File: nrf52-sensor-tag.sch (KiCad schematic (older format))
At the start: 20 parts, among them IC1 ISP1807-LR-RS, IC2 MAX44009EDT+T, U1 BME280

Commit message: Moved components and routed the board
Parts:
- removed R?: 10k, Resistor_SMD:R_0603_1608Metric, symbol Device:R_Small
- removed U?: MAX811REUS-T, Package_TO_SOT_SMD:SOT-143, symbol Power_Supervisor:MAX811REUS-T
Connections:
- net labels removed: BATLOW
- wire segments 76 -> 70
- no-connect marks 40 -> 39
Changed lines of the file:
@@
 Wire Wire Line
 	5050 3500 5300 3500
-$Comp
-L Power_Supervisor:MAX811REUS-T U?
-U 1 1 601F6A74
-P 5350 6600
-F 0 "U?" H 5600 7000 50  0000 L CNN
-F 1 "MAX811REUS-T" H 5500 6900 50  0000 L CNN
-F 2 "Package_TO_SOT_SMD:SOT-143" H 5450 6300 50  0001 L CNN
-F 3 "https://datasheets.maximintegrated.com/en/ds/MAX811-MAX812.pdf" H 5000 5900 50  0001 C CNN
-	1    5350 6600
-	1    0    0    -1
-$EndComp
-Text Label 6150 6600 2    50   ~ 0
-BATLOW
-Wire Wire Line
-	6150 6600 5750 6600
-Text Label 5150 6200 0    50   ~ 0
-VCC
-Wire Wire Line
-	5150 6200 5350 6200
-Wire Wire Line
-	5350 6200 5350 6300
-NoConn ~ 4950 6600
-$Comp
-L power:GND #PWR?
-U 1 1 601FE059
-P 5350 6900
-F 0 "#PWR?" H 5350 6650 50  0001 C CNN
-F 1 "GND" H 5355 6727 50  0000 C CNN
-F 2 "" H 5350 6900 50  0001 C CNN
-F 3 "" H 5350 6900 50  0001 C CNN
-	1    5350 6900
-	1    0    0    -1
-$EndComp
-$Comp
-L Device:R_Small R?
-U 1 1 601FEA86
-P 6250 5750
-F 0 "R?" V 6054 5750 50  0000 C CNN
-F 1 "10k" V 6145 5750 50  0000 C CNN
-F 2 "Resistor_SMD:R_0603_1608Metric" H 6250 5750 50  0001 C CNN
-F 3 "~" H 6250 5750 50  0001 C CNN
-	1    6250 5750
-	0    1    1    0
-$EndComp
-Text Label 5750 5750 0    50   ~ 0
-BATLOW
-$Comp
-L power:GND #PWR?
-U 1 1 601FEFB1
-P 6600 5800
-F 0 "#PWR?" H 6600 5550 50  0001 C CNN
-F 1 "GND" H 6605 5627 50  0000 C CNN
-F 2 "" H 6600 5800 50  0001 C CNN
-F 3 "" H 6600 5800 50  0001 C CNN
-	1    6600 5800
-	1    0    0    -1
-$EndComp
-Wire Wire Line
-	5750 5750 6150 5750
-Wire Wire Line
-	6350 5750 6600 5750
-Wire Wire Line
-	6600 5750 6600 5800
 $EndSCHEMATC

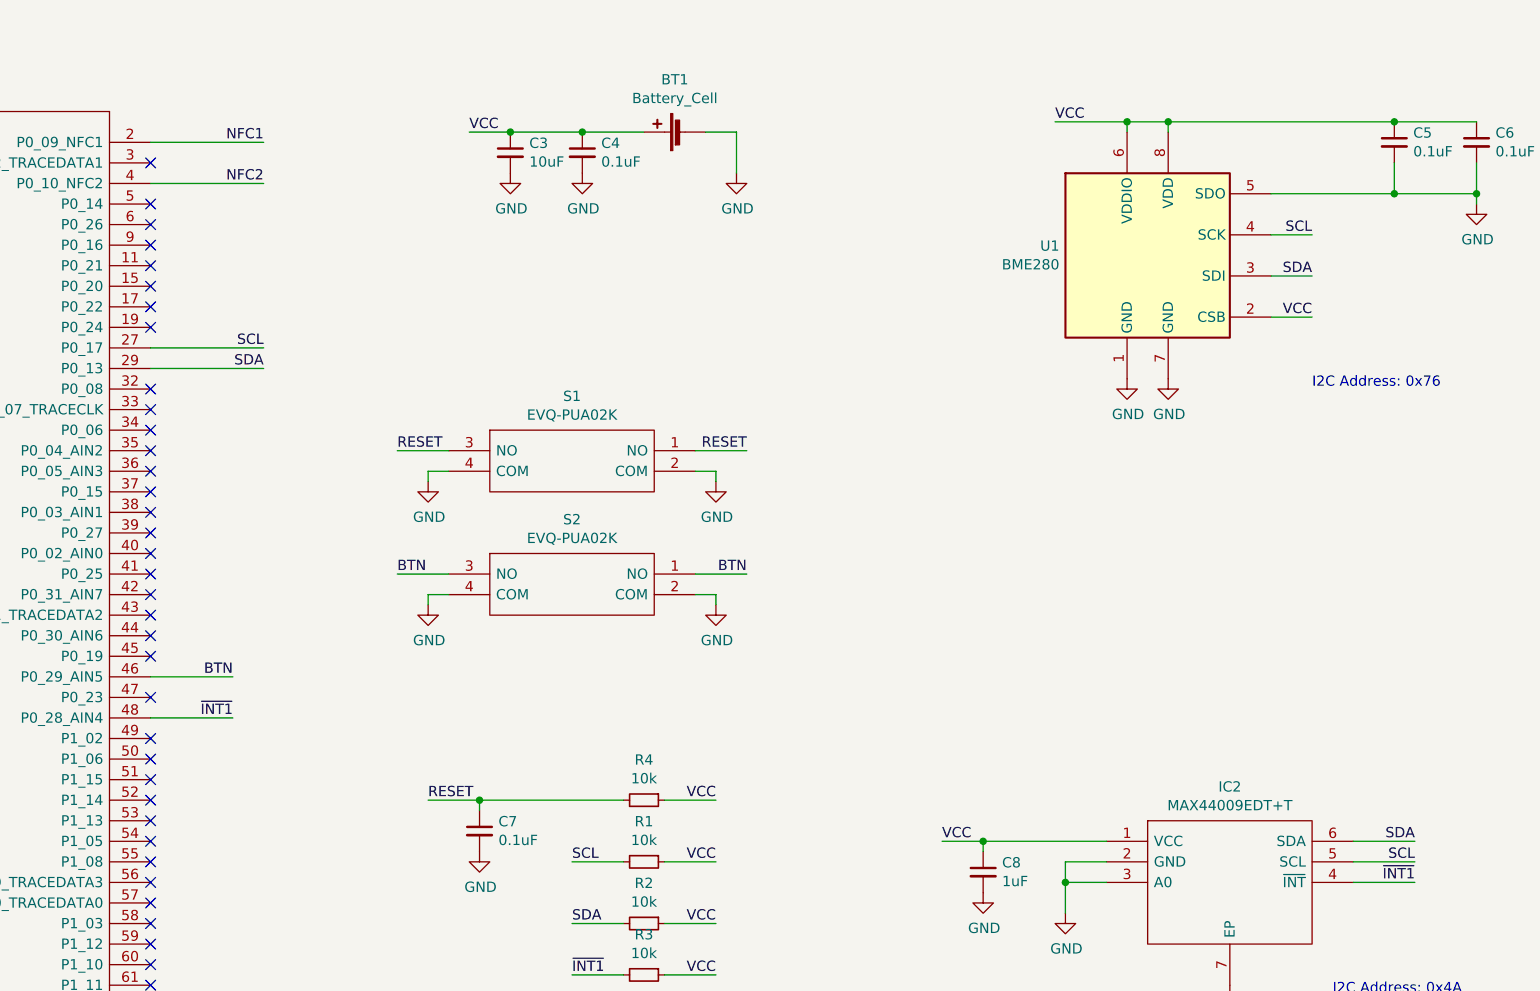
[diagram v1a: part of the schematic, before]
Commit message: Attached the sensors VCC to GPIOs of the nrf instead vcc (incl. a jumper just in case)
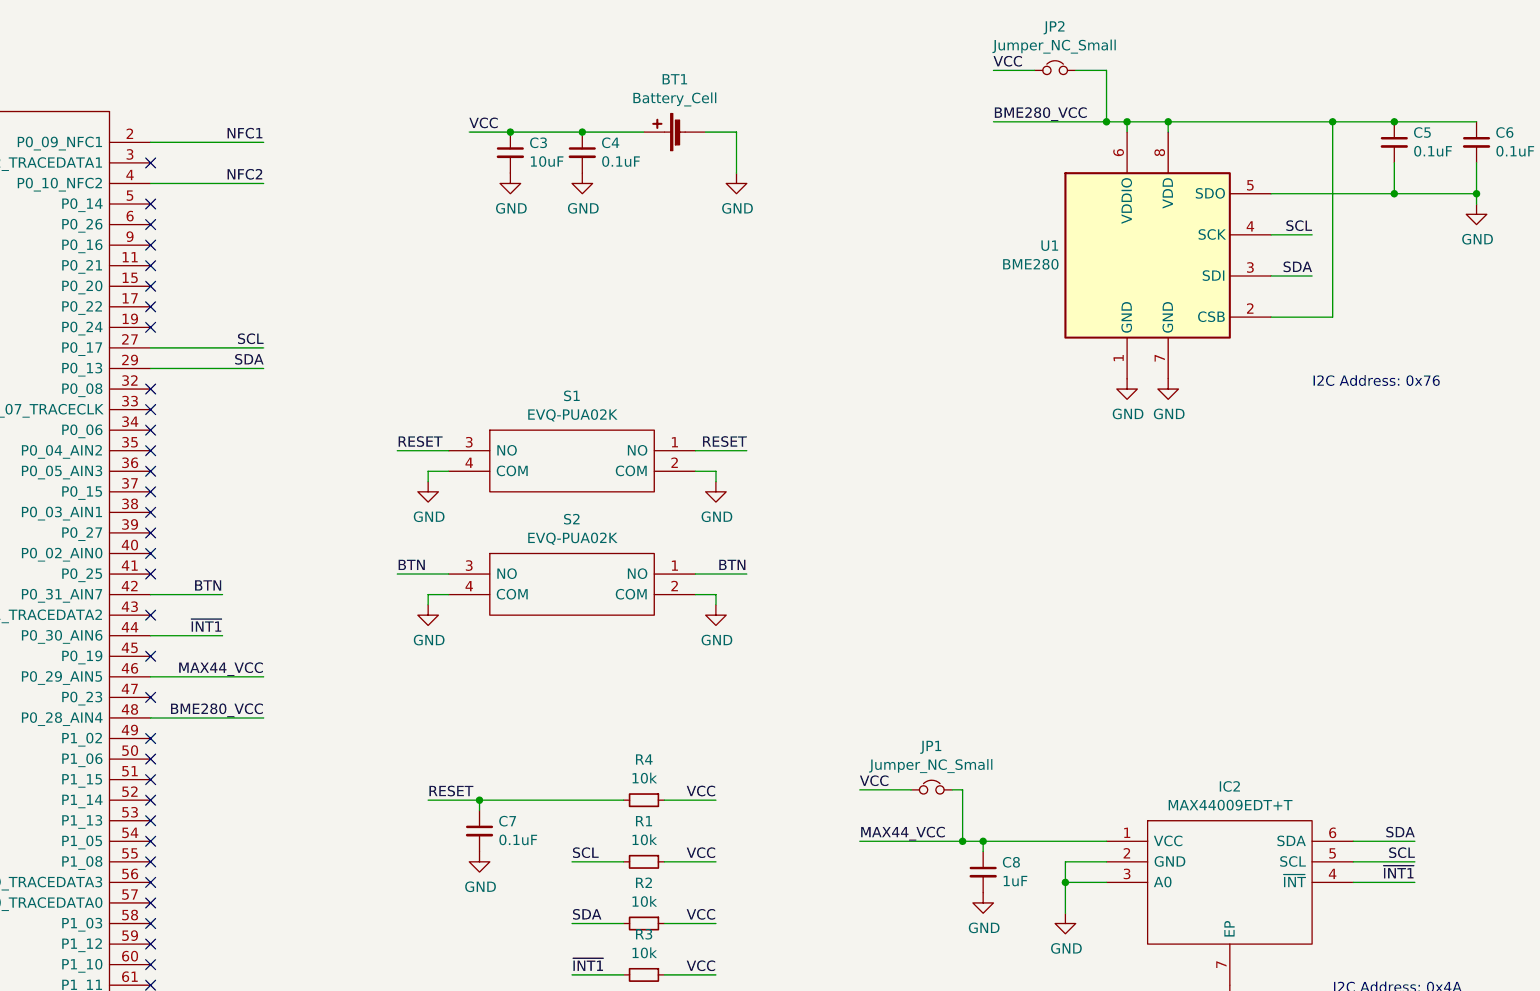
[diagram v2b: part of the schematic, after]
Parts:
- added JP1, JP2: Jumper_NC_Small, Jumper:SolderJumper-2_P1.3mm_Open_TrianglePad1.0x1.5mm, symbol Device:Jumper_NC_Small
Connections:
- net BTN: now also IC1.42 (P0_31_AIN7); no longer IC1.46 (P0_29_AIN5)
- net VCC: now also JP1.1, JP2.1; no longer C5.1, C6.1, C8.1, IC2.1 (VCC), U1.2 (CSB), U1.6 (VDDIO), U1.8 (VDD)
- net ~INT1: now also IC1.44 (P0_30_AIN6); no longer IC1.48 (P0_28_AIN4)
- new net BME280_VCC: C5.1, C6.1, IC1.48 (P0_28_AIN4), JP2.2, U1.2 (CSB), U1.6 (VDDIO), U1.8 (VDD)
- new net MAX44_VCC: C8.1, IC1.46 (P0_29_AIN5), IC2.1 (VCC), JP1.2
- no-connect marks 39 -> 37
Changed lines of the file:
@@
 	1    0    0    -1
 $EndComp
-Text Label 8250 1300 0    50   ~ 0
-VCC
+Text Label 7950 1300 0    50   ~ 0
+BME280_VCC
 Wire Wire Line
 	8600 1350 8600 1300
-Wire Wire Line
-	8600 1300 8250 1300
 Wire Wire Line
 	8800 1350 8800 1300
@@
 	8600 1300 8800 1300
 Wire Wire Line
-	8800 1300 9900 1300
+	8800 1300 9600 1300
 Connection ~ 8800 1300
 Connection ~ 9900 1300
@@
 Text Label 6600 5200 2    50   ~ 0
 VCC
-Text Label 9500 2250 2    50   ~ 0
-VCC
-Wire Wire Line
-	9500 2250 9300 2250
 Wire Wire Line
 	5900 4900 6150 4900
@@
 Wire Wire Line
 	6600 4900 6350 4900
-Text Label 7700 4800 0    50   ~ 0
-VCC
+Text Label 7300 4800 0    50   ~ 0
+MAX44_VCC
 $Comp
 L power:GND #PWR0105
@@
 	1    0    0    -1
 $EndComp
-Wire Wire Line
-	7700 4800 7900 4800
 Wire Wire Line
 	7900 4850 7900 4800
@@
 NoConn ~ 3850 3400
 NoConn ~ 3850 3500
-NoConn ~ 3850 3600
 NoConn ~ 3850 3700
-NoConn ~ 3850 3800
 NoConn ~ 3850 3900
 NoConn ~ 3850 4100
@@
 NoConn ~ 3850 5700
 NoConn ~ 3850 5800
-Text Label 4250 4200 2    50   ~ 0
+Text Label 4200 3800 2    50   ~ 0
 ~INT1
-Wire Wire Line
-	4250 4200 3850 4200
 $Comp
 L EVQ-PUA02K:EVQ-PUA02K S1
@@
 	1    0    0    -1
 $EndComp
-Text Label 4250 4000 2    50   ~ 0
+Text Label 4200 3600 2    50   ~ 0
 BTN
-Wire Wire Line
-	4250 4000 3850 4000
 Text Label 6750 3500 2    50   ~ 0
 BTN
@@
 Wire Wire Line
 	5050 3500 5300 3500
+Wire Wire Line
+	7950 1300 8500 1300
+Wire Wire Line
+	4200 3600 3850 3600
+Wire Wire Line
+	4200 3800 3850 3800
+Text Label 4400 4000 2    50   ~ 0
+MAX44_VCC
+Text Label 4400 4200 2    50   ~ 0
+BME280_VCC
+Wire Wire Line
+	3850 4200 4400 4200
+Wire Wire Line
+	3850 4000 4400 4000
+$Comp
+L Device:Jumper_NC_Small JP2
+U 1 1 6023FE8E
+P 8250 1050
+F 0 "JP2" H 8250 1262 50  0000 C CNN
+F 1 "Jumper_NC_Small" H 8250 1171 50  0000 C CNN
+F 2 "Jumper:SolderJumper-2_P1.3mm_Open_TrianglePad1.0x1.5mm" H 8250 1050 50  0001 C CNN
+F 3 "~" H 8250 1050 50  0001 C CNN
+	1    8250 1050
+	1    0    0    -1
+$EndComp
+$Comp
+L Device:Jumper_NC_Small JP1
+U 1 1 60240E97
+P 7650 4550
+F 0 "JP1" H 7650 4762 50  0000 C CNN
+F 1 "Jumper_NC_Small" H 7650 4671 50  0000 C CNN
+F 2 "Jumper:SolderJumper-2_P1.3mm_Open_TrianglePad1.0x1.5mm" H 7650 4550 50  0001 C CNN
+F 3 "~" H 7650 4550 50  0001 C CNN
+	1    7650 4550
+	1    0    0    -1
+$EndComp
+Text Label 7300 4550 0    50   ~ 0
+VCC
+Wire Wire Line
+	7300 4550 7550 4550
+Wire Wire Line
+	7300 4800 7800 4800
+Wire Wire Line
+	7750 4550 7800 4550
+Wire Wire Line
+	7800 4550 7800 4800
+Connection ~ 7800 4800
+Wire Wire Line
+	7800 4800 7900 4800
+Text Label 7950 1050 0    50   ~ 0
+VCC
+Wire Wire Line
+	7950 1050 8150 1050
+Wire Wire Line
+	8350 1050 8500 1050
+Wire Wire Line
+	8500 1050 8500 1300
+Connection ~ 8500 1300
+Wire Wire Line
+	8500 1300 8600 1300
+Wire Wire Line
+	9600 2250 9600 1300
+Wire Wire Line
+	9300 2250 9600 2250
+Connection ~ 9600 1300
+Wire Wire Line
+	9600 1300 9900 1300
 $EndSCHEMATC

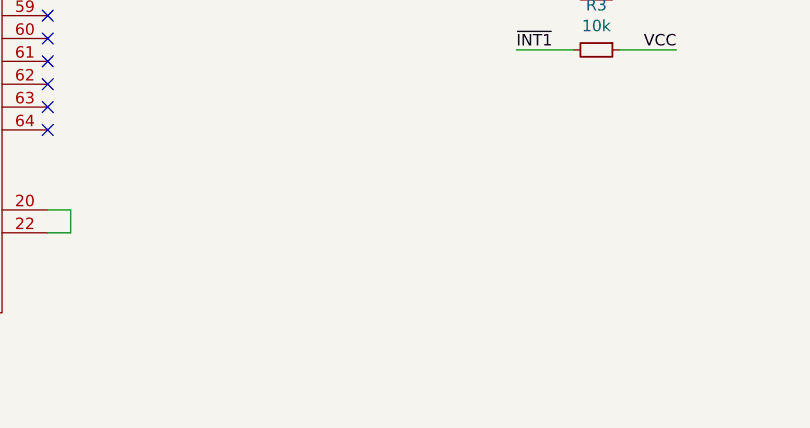
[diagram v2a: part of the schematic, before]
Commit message: Add debug connector
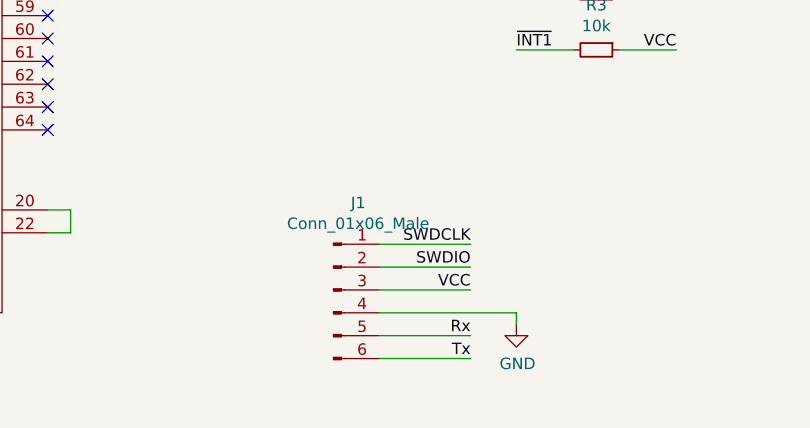
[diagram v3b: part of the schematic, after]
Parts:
- added J1: Conn_01x06_Male, Connector_PinHeader_2.00mm:PinHeader_1x06_P2.00mm_Vertical, symbol Connector:Conn_01x06_Male
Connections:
- net GND: now also J1.4 (Pin_4)
- net SWDCLK: now also J1.1 (Pin_1)
- net SWDIO: now also J1.2 (Pin_2)
- net VCC: now also J1.3 (Pin_3)
- new net Rx: J1.5 (Pin_5)
- new net Tx: J1.6 (Pin_6)
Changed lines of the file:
@@
 Wire Wire Line
 	9600 1300 9900 1300
+$Comp
+L Connector:Conn_01x06_Male J1
+U 1 1 6020A1D2
+P 5100 6500
+F 0 "J1" H 5208 6881 50  0000 C CNN
+F 1 "Conn_01x06_Male" H 5208 6790 50  0000 C CNN
+F 2 "Connector_PinHeader_2.00mm:PinHeader_1x06_P2.00mm_Vertical" H 5100 6500 50  0001 C CNN
+F 3 "~" H 5100 6500 50  0001 C CNN
+	1    5100 6500
+	1    0    0    -1
+$EndComp
+Text Label 5700 6400 2    50   ~ 0
+SWDIO
+Text Label 5700 6300 2    50   ~ 0
+SWDCLK
+Text Label 5700 6500 2    50   ~ 0
+VCC
+$Comp
+L power:GND #PWR0118
+U 1 1 6020BEB6
+P 5900 6650
+F 0 "#PWR0118" H 5900 6400 50  0001 C CNN
+F 1 "GND" H 5905 6477 50  0000 C CNN
+F 2 "" H 5900 6650 50  0001 C CNN
+F 3 "" H 5900 6650 50  0001 C CNN
+	1    5900 6650
+	1    0    0    -1
+$EndComp
+Wire Wire Line
+	5300 6600 5900 6600
+Wire Wire Line
+	5700 6500 5300 6500
+Wire Wire Line
+	5300 6400 5700 6400
+Wire Wire Line
+	5700 6300 5300 6300
+Wire Wire Line
+	5900 6650 5900 6600
+Text Label 5700 6800 2    50   ~ 0
+Tx
+Text Label 5700 6700 2    50   ~ 0
+Rx
+Wire Wire Line
+	5700 6700 5300 6700
+Wire Wire Line
+	5700 6800 5300 6800
 $EndSCHEMATC

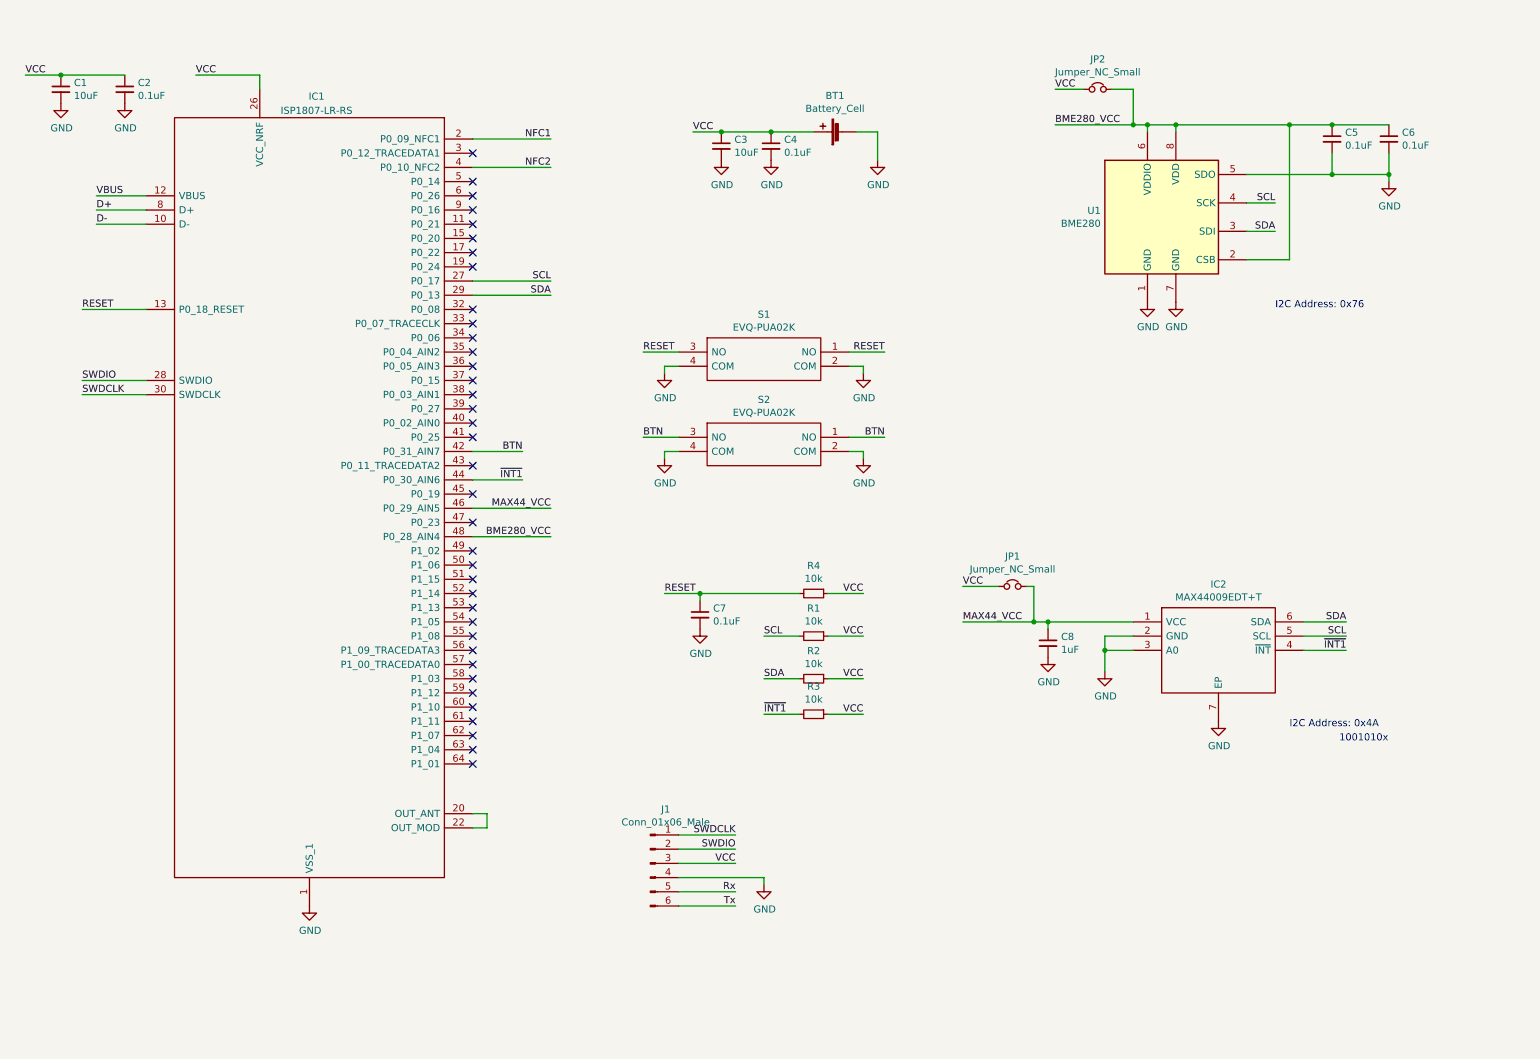
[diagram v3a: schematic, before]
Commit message: Beautify schematics + added debug connector
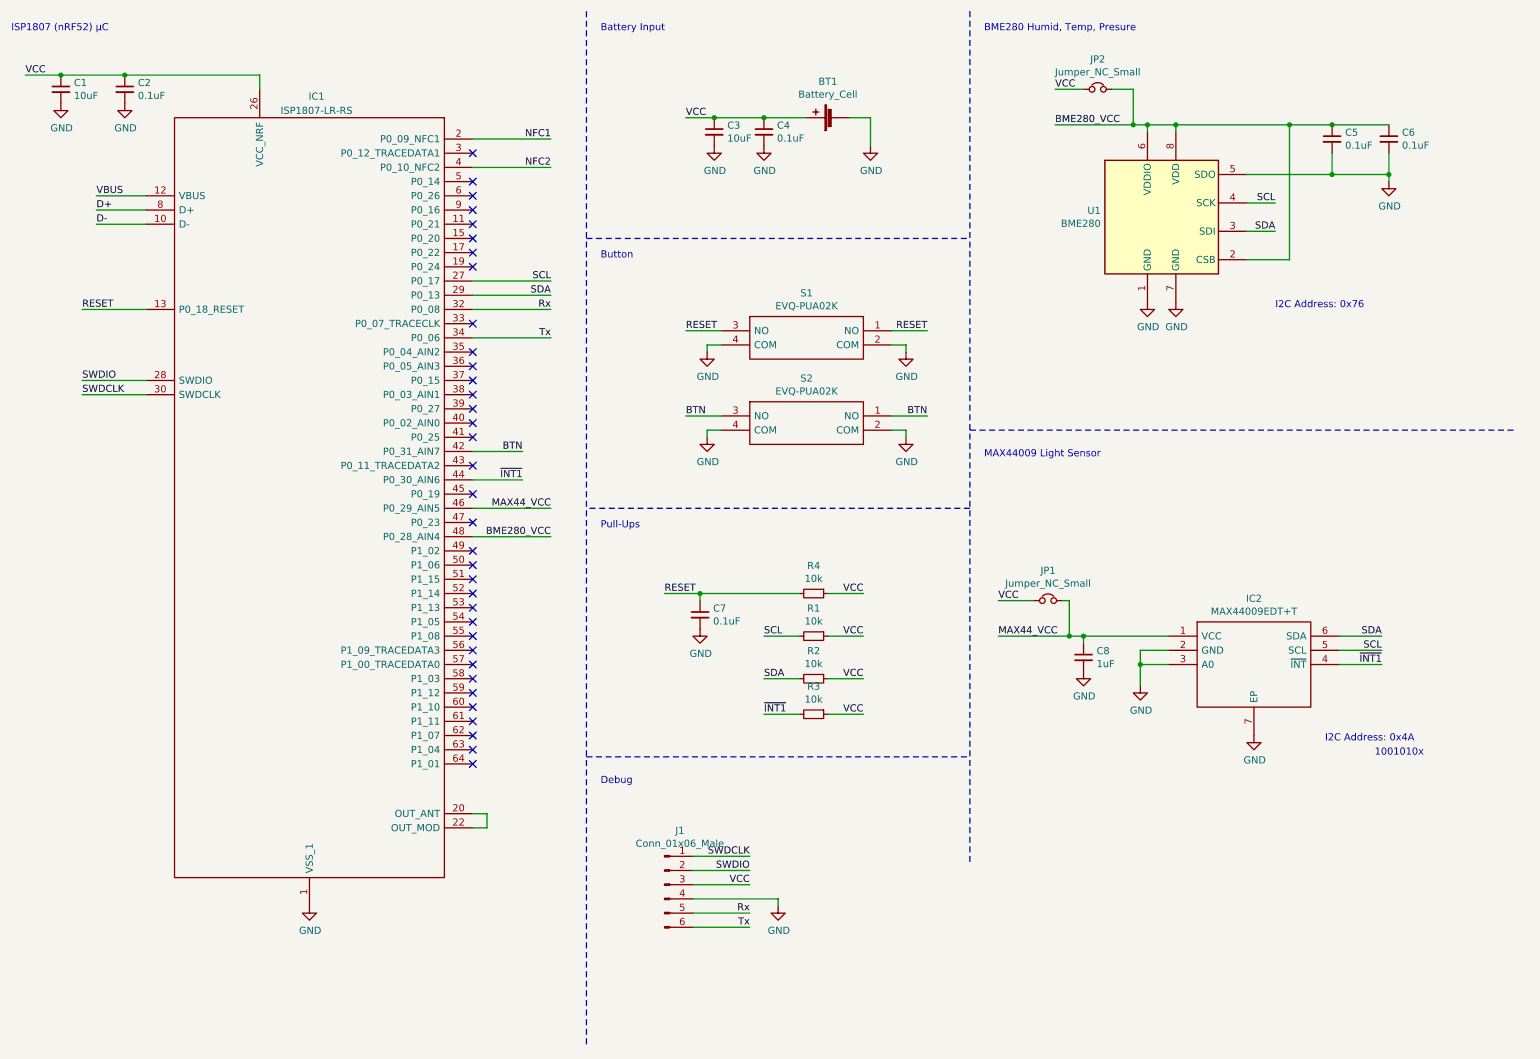
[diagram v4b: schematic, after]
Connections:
- net Rx: now also IC1.32 (P0_08)
- net Tx: now also IC1.34 (P0_06)
- no-connect marks 37 -> 35
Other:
- note added: "BME280 Humid, Temp, Presure"
- note added: "Battery Input"
- note added: "Button"
- note added: "Debug"
- note added: "ISP1807 (nRF52) µC"
- note added: "MAX44009 Light Sensor"
- note added: "Pull-Ups"
- moved on the sheet: BT1, C3, C4, C8, IC2, J1, JP1, S1, S2
